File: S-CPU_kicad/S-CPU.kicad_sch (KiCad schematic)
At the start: 400 parts, among them U10 TRI_BUF_IF1, U11 TRI_BUF_IF1, U12 TRI_BUF_IF1, U13 TRI_BUF_IF1, U14 TRI_BUF_IF1, U18 HAUU1, U19 HAUU0, U20 TRI_BUF_IF1, U21 TRI_BUF_IF1, U22 TRI_BUF_IF1, U6 IAOO1, U8 IAOO0

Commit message: Fixed complex gate names. Most fo the cells in the mul div section have been idnetified in SVG file.
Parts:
- BBZX, FBAC: value AND_4_NOR_2 -> AOI_14; symbol Ricoh_Cells:AND_4_NOR_2 -> Ricoh_Cells:AOI_14
- BCDB, OCDM: value AND_3_AND_3_NOR_2 -> AOI_33; symbol Ricoh_Cells:AND_3_AND_3_NOR_2 -> Ricoh_Cells:AOI_33
- CABL, JBNA, KAQE: value OR_2_NAND_3 -> OAI_112; symbol Ricoh_Cells:OR_2_NAND_3 -> Ricoh_Cells:OAI_112
- HAUU1: renamed from U18; value HAUU1 -> MUX
- MBUP: value AND_4_NOR_2 -> AOI_22; symbol Ricoh_Cells:AND_2_AND_2_NOR_2 -> Ricoh_Cells:AOI_22
- OBNU: value OR_2_OR_2_OR_2_OR_2_NAND_4 -> OAI_2222; symbol Ricoh_Cells:OR_2_NAND_4 -> Ricoh_Cells:OAI_2222
- UHAUU0: renamed from U19; value HAUU0 -> MUX
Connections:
- net wJBQK: now also OBNU.2; no longer OBNU.7
- net wOCOG_~{MODE7}: now also OBNU.4; no longer OBNU.5
- net ~{MODE0}: now also OBNU.6; no longer OBNU.3
- net ~{MODE1}: now also OBNU.8; no longer OBNU.1
- net ~{wRDY}: now also OBNU.5, OBNU.7; no longer OBNU.2, OBNU.4
- net at OBEA.2: now also OBNU.3; no longer OBNU.6
- net at OBXF.2: now also OBNU.1; no longer OBNU.8
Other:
- added sheet MULTIPLICATION & DIVISION REGISTERS (muldiv.kicad_sch)
- note removed: "420X To bottom section for all registers execpt 420D"
- moved on the sheet: ACLK, BAEW, BAFF, BANP, BANW, BANX, BAOZ, BAPI, BAYS, BBAR, CABL, CAZC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

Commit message: Latch cell identified. Progress in Mul Div section.
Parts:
- removed HAMT: TRI_BUF_IF0, symbol Ricoh_Cells:TRI_BUF_IF0
- removed IBSM, LBXR: TRI_BUF_IF1, symbol Ricoh_Cells:TRI_BUF_IF1
- added HAMT, IBSM, LBXR: D_LATCH_A2, symbol Ricoh_Cells:D_LATCH_A2
- KAQE: value OAI_112 -> OAI_13; symbol Ricoh_Cells:OAI_112 -> Ricoh_Cells:OAI_13
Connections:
- net 65816_RW: now also IBSM.2 (D)
- net DMA_ON?: now also LBXR.2 (D)
- net wLCIH: now also HAMT.1 (~{ENA}), HAMT.3 (ENA), IBSM.1 (~{ENA}), IBSM.3 (ENA)
- net wNBHM: now also LBXR.1 (~{ENA}), LBXR.3 (ENA)
- net at JBNA.1: now also LBXR.4 (Q)
- net at IBPD.1 (IN), IBPD.3 (IN): now also IBSM.4 (Q)
- net at HALC.1: now also HAMT.4 (Q)
- net at HALC.2, HANA.2: now also HAMT.2 (D)
- net OAGE: now reaches OAGE.2
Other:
- note added: "CLK/8?"
- note removed: "CLK/8 Goes to DMA"
- moved on the sheet: ACLK, DBPP, IBPD, KAQE, KBNZ, OAGE

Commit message: More MUL DIV section updates,
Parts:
- added MCCZ1, MCCZ?: OR_2, symbol Ricoh_Cells:OR_2
- added MCCZ?: INVERTER_A, symbol Ricoh_Cells:INVERTER_A
- OAUS: symbol Ricoh_Cells:TRI_BUF_IF1 -> Ricoh_Cells:TRI_BUF_IF0
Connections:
- net DMA_CLK?: now also MCCZ?.1
- net ~{CPU_RD}: now also MCCZ?.2
- net ~{MAWK_WR}: now also MCCZ1.2
- net wMASS renamed wMASS_RST
- new net: MCCZ1.1, MCCZ?.1, MCCZ?.2
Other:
- sheet MULTIPLICATION & DIVISION REGISTERS renamed DIVISION QUOTIENT REGISTERS
- added sheet MUL PRODUCT OR DIV REMAINDER REGISTERS (productremainder.kicad_sch)
- sheet ADDR_AND_DATA_BUSES: file untitled.kicad_sch -> addrdatabuses.kicad_sch
- sheet DIVISION QUOTIENT REGISTERS: file muldiv.kicad_sch -> divquotient.kicad_sch
- sheet DIVISION QUOTIENT REGISTERS ports: added 4202_WR, DIV_ON, DIV_OR_MUL_ON, DO_ADD_SUB, D[0..7], MUL_DIV_CLK_4203_WR, OAGE, ZDIV, wDBJW_wHASI_RST, wKBNZ, ~{4203_WR}, ~{4203}, ~{4206_WR}, ~{4206}, ~{4214_RD}, ~{4215_RD}; removed none
- sheet JOYPADS REGISTERS ports: added AUTO_JP_EN, wMASS_RST, wNBRL_wNBQA_XIN/4, wOCOG_~{MODE7}, ~{4016}, ~{4017}, ~{wRDY}; removed wMASS
- sheet OTHER_42XX_REGISTERS ports: added 4202_WR, 4204_WR, 4205_WR, wVBLANK, ~{4203_WR}, ~{4203}, ~{4206_WR}, ~{4206}, ~{4214_RD}, ~{4215_RD}, ~{4216_RD}, ~{4217_RD}; removed none
- note added: "DMA"
- note added: "Disconnects 65816 in MODE7, in MODE1 when RDY is low and during DMA"
- note added: "Modes are active low - inputs seems to be active low MODE7 = Test mode with external CPU connections bypassing 65816 MODE4-6 = DMA test modes MODE0 = SNES mode MODE1 = SNES in halt mode where RDY is used to pause the 65816 MODE2-3 = NES modes where 4200-43FF registers are disabled"
- note added: "When wJBDJ is set to 0 it might force 6502 emulation mode since wJBDJ can only be low in MODE 2 or 3"
- note removed: "Disconnects 65816 in MODE7, in MODE1 when RDY is low and during DMA Works with LCIH HAMT and IBSM might be inverting tri buffers for this to make sense."
- note removed: "Modes are active low - inputs seems to be active low MODE7 = Test mode with external CPU connections bypassing 65816 MODE4-6 = DMA test modes MODE2-3 = NES modes where 4200-43FF registers are disabled MODE0-1 = SNES modes"

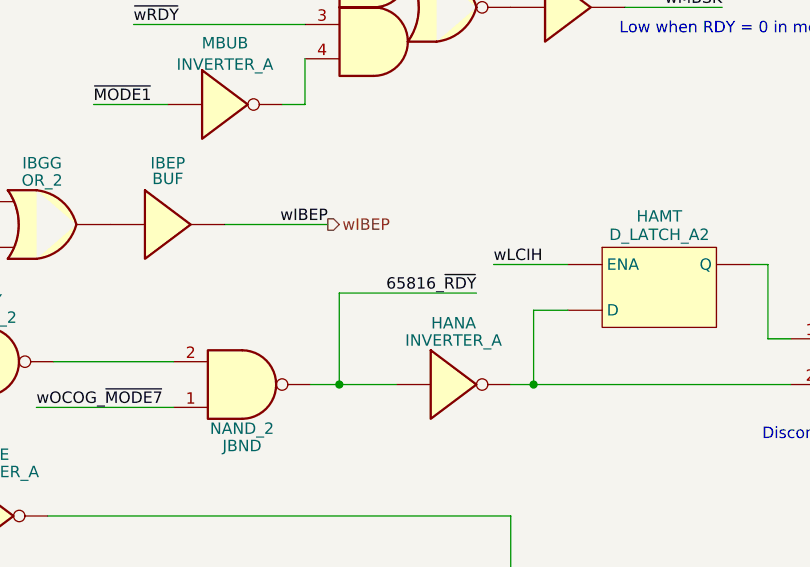
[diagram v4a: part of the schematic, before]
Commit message: D latch with reset and tri state output identified
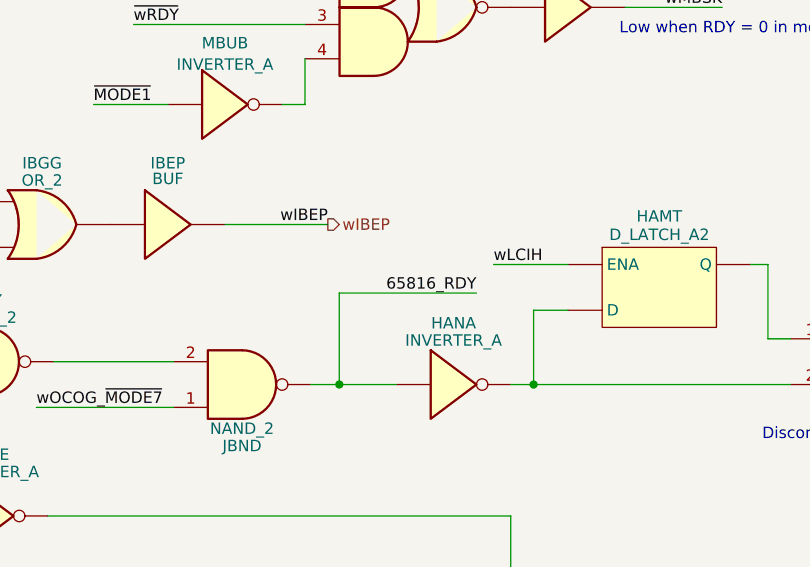
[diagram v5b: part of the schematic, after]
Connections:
- net 65816_~{RDY} renamed 65816_RDY
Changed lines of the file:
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@@
     (effects (font (size 1.27 1.27)) (justify right bottom))
   )
-  (label "65816_~{RDY}" (at 956.31 622.935 180) (fields_autoplaced)
+  (label "65816_RDY" (at 956.31 622.935 180) (fields_autoplaced)
     (effects (font (size 1.27 1.27)) (justify right bottom))
   )

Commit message: ADDR and DAT bus progress
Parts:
- removed ABRB: TRI_INV_IF2, symbol Ricoh_Cells:TRI_INV_IF2
- removed ACOU, U10, U11, U12, U13, U14, U20, U21, U22: TRI_BUF_IF1, symbol Ricoh_Cells:TRI_BUF_IF1
- removed GBTC, IBPR: INVERTER_A, symbol Ricoh_Cells:INVERTER_A
- removed GBTL: BUF, symbol Ricoh_Cells:BUF
- removed IBPD: TRI_BUF_IF0, symbol Ricoh_Cells:TRI_BUF_IF0
- removed IBSM: D_LATCH_A2, symbol Ricoh_Cells:D_LATCH_A2
- removed JBQV, JBRI: AND_2, symbol Ricoh_Cells:AND_2
- removed RW: IOBUF_A, symbol Ricoh_Cells:IOBUF_A
- HBCA, HBEP: value TRI_BUF_IF1 -> TRI_INV_IF0; symbol Ricoh_Cells:TRI_BUF_IF1 -> Ricoh_Cells:TRI_INV_IF0
- VDA, VPA: value IOBUF_A -> IOBUF_B; symbol Ricoh_Cells:IOBUF_A -> Ricoh_Cells:IOBUF_B
- renumbered DBHA to DADO, NBRL to NBWJ
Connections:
- net wJAXC is gone; now on an unnamed net: DCEG.1 (~{ENA}), FBSI.1 (~{ENA})
- net DMA_CLK?: no longer MCCZ?.1
- net wIARB_or_wHBCA: now also HBCA.3; no longer HBCA.4
- net wIOAW_or_wHBEP: now also HBEP.3; no longer HBEP.4
- net at DCEG.3: now also VPA.4 (~{DRV}_HIGH); no longer VPA.3 (~{DRV}_HIGH)
- net at FBSI.3: now also VDA.4 (~{DRV}_HIGH); no longer VDA.3 (~{DRV}_HIGH)
- net DATABUS_LATCH: now reaches ODSN.2
- net MODE0_OR_MODE1_AND_RDY: now reaches JAXB.1, JBNA.4, JBPY.1, KBUP.3
- net 21XX_DMA_RD? renamed 21XX_DMA_RD
- net AAA renamed DMA_OFF
- net DMA_OFF: now also MCCZ?.1
- net DIR_OUT_EN renamed ~{INTERNAL_ADDR_EN}
- net ODQC renamed DATAIN_EN
- net wBCDB renamed ~{DMA_RD}
- net wHAKW renamed ~{65816_ADDR_EN}
- net wIBEP renamed ~{65816_ADDR_RST}
- net wLCIH renamed 65816_ADDR_LATCH
- net wMBSK renamed ~{EXTERNAL_BUS_EN}
- net wODIB renamed DATAOUT_EN
- net ~{21XX_DMA_RD?} renamed ~{21XX_DMA_RD}
- net ~{21XX_DMA_WR?} renamed ~{21XX_DMA_WR}
- net ~{MODE0-3_OR_MODE7} renamed MODE4-6
- net ~{WR}: no longer names the net of BBZX.3, HAXK.1, JBCR.1
- new net: HAZL.2, HBCA.1 (~{ENA}), HBEP.1 (~{ENA})
- new net: HBCA.2, HBCT.3
- new net: HBEP.2, HBGA.3
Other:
- sheet ADDR_AND_DATA_BUSES ports: added 65816_ADDR_LATCH, 65816_A[0..23], 65816_RW, A[0..23], DATABUS_LATCH, DATAIN_EN, DATAOUT_EN, DMA_A[0..23], MODE2_OR_MODE3, RW, ~{65816_ADDR_EN}, ~{65816_ADDR_RST}, ~{EXTERNAL_BUS_EN}, ~{INTERNAL_ADDR_EN}; removed none
- note added: "CPU clock (1 -> 0)"
- note added: "Connected to Data OUT Bus enable pins ODIB = '0' to present data to external bus"
- note added: "Connected to Data OUT Bus enable pins ODQC = '0' to read external data bus"
- note added: "DMA OFF CPU CLK"
- note added: "Internal registers only"
- note added: "JBNA = JBQK set to '1' when in MODE2-3, in MODE7, in MODE1 + RDY = 0 or DMA is on?"
- note added: "Latches 65816 Addresses on first half of CPU clock period, normally off during DMA and permanently latched in MODE7"
- note added: "Latches exernal input data and data bus"
- note added: "Low when RDY = 0 in mode 1 or when DMA is on in mode 4-6"
- note added: "Modes are active low - inputs seems to be active low MODE7 = Test mode with external CPU connections bypassing 65816 MODE4-6 = DMA test modes MODE0 = SNES mode MODE1 = SNES in halt mode where RDY is used to pause the 65816 MODE2-3 = NES modes where 4200-43FF registers are disabled and CPU connections are external as original idea was probably to include the NES CPU on the board"
- note removed: "CLK/8?"
- note removed: "Connected to Data IN Bus enable pins"
- note removed: "Connected to Data OUT Bus enable pins"
- note removed: "Enables 65816 Addresses when OCOG is low MODE7, external ADDRESS and DATA"
- note removed: "Latch signal for readable registers?"
- note removed: "Low when RDY = 0 in mode 1 or mode 4-6 and DMA on"
- note removed: "Modes are active low - inputs seems to be active low MODE7 = Test mode with external CPU connections bypassing 65816 MODE4-6 = DMA test modes MODE0 = SNES mode MODE1 = SNES in halt mode where RDY is used to pause the 65816 MODE2-3 = NES modes where 4200-43FF registers are disabled"
- note removed: "enables a Data bus IO buffers on end of row O"
- moved on the sheet: BAAO, BBER, BBNW, BBZX, DCEG, FBSI, HAKW, HALC, HALT, HAMT, HANA, HAXK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

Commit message: DMA progress. Most gates identified.
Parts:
- renumbered DRAMMODE to ~{DRAMMODE}
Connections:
- net DMA_ON is gone; now on net DMA_ON?: JAXO.1, JBSU.1, MAXX.1
- net XIN: now also CAKS.1 (~{RESET}), CAKS.5 (~{RESET}), CAKW.1 (~{RESET}), CAKW.5 (~{RESET}), CANH.1 (~{RESET}), CANH.5 (~{RESET}), CAQL.1 (~{RESET}), CAQL.5 (~{RESET}), CBDC.1 (~{RESET}), CBDC.5 (~{RESET}), CBEP.1 (~{RESET}), CBEP.5 (~{RESET}), CBFI.1 (~{RESET}), CBFI.5 (~{RESET}), CBGC.1 (~{RESET}), CBGC.5 (~{RESET}), DBJW.1, HASI.1, IAUO.6 (Q), IAYI.2 (D)
- net wIARF renamed ~{INTERNAL_CYCLE}
- net wPASU renamed REFRESH_EN
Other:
- added sheet DMA (dma.kicad_sch)
- note added: "~{0000-1FFF} is WRAM ~{6000-7FFF} is expansion ~{4000-41FF} is controller 0000-7FFF is IO range BOAZ is low when accessing 2000-3FFF range (PPU, APU) and 4200-5FFF range (CPU + DMA) BANP is low when A23 is high but not in IO range i.e. FAST ROM access Therefore CABL will be high to allow 6 master cycles per cpu cycle when CPU accesses fast rom, some IO registers and during internal cycles (provid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"
- note removed: "~{0000-1FFF} is WRAM ~{6000-7FFF} is expansion ~{4000-41FF} is controller 0000-7FFF is IO range BOAZ is low when accessing 2000-3FFF range (PPU, APU) and 4200-5FFF range (CPU + DMA) BANP is low when A23 is high but not in IO range i.e. FAST ROM access Therefore CABL will be high to allow 6 master cycles per cpu cycle when CPU accesses fast rom, some IO registers + other cases handled by GBEB stil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"
- moved on the sheet: AABZ, AAHT, AAJX, AAKO, AAMX, ACLK, ACPQ, BABK, BABL, BAEW, BAFF, BANP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
